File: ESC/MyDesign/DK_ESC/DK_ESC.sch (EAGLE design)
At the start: 61 parts, among them IC2 7805

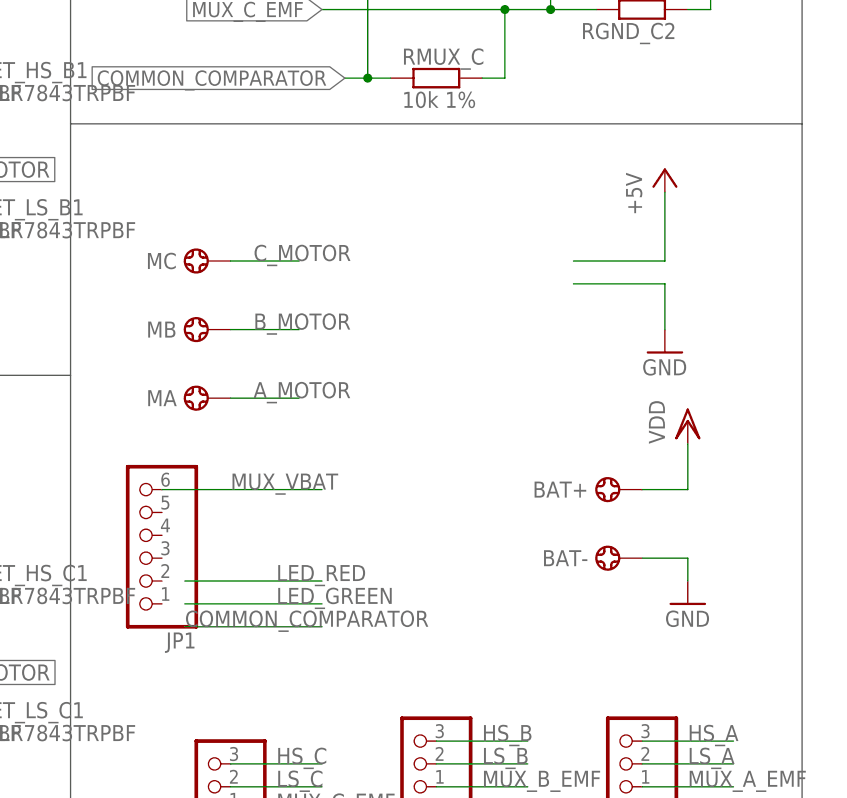
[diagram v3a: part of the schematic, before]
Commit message: Finish layout test ESC
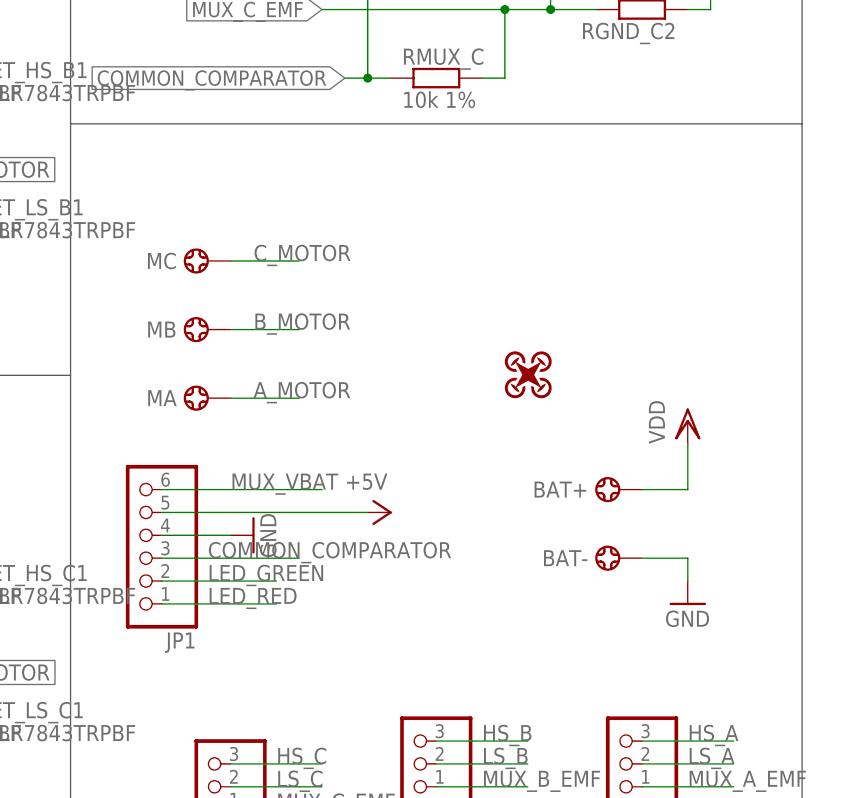
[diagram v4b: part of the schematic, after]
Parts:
- added U$2: QUADCOPTER-MEDIUM, logo:QUADCOPTER-MEDIUM
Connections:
- net +5V: now also JP1.5
- net COMMON_COMPARATOR: now also JP1.3
- net GND: now also JP1.4
- net LED_GREEN: now also JP1.2
- net LED_RED: now also JP1.1
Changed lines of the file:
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@@
 <part name="JP-C" library="pinhead" deviceset="PINHD-1X3" device=""/>
 <part name="JP1" library="pinhead" deviceset="PINHD-1X6" device=""/>
+<part name="U$2" library="logo" deviceset="QUADCOPTER" device="-MEDIUM"/>
 </parts>
 <sheets>
@@
 <instance part="MB" gate="G$1" x="96.52" y="-35.56" rot="R180"/>
 <instance part="MC" gate="G$1" x="96.52" y="-27.94" rot="R180"/>
-<instance part="GND11" gate="1" x="147.32" y="-38.1"/>
-<instance part="P+6" gate="1" x="147.32" y="-17.78"/>
+<instance part="GND11" gate="1" x="101.6" y="-58.42" rot="R90"/>
+<instance part="P+6" gate="1" x="116.84" y="-55.88" rot="R270"/>
 <instance part="FET_HS_A1" gate="G$1" x="66.04" y="45.72"/>
 <instance part="FET_LS_A1" gate="G$1" x="66.04" y="30.48"/>
@@
 <instance part="JP-C" gate="A" x="96.52" y="-86.36" rot="R180"/>
 <instance part="JP1" gate="A" x="88.9" y="-58.42" rot="R180"/>
+<instance part="U$2" gate="G$1" x="129.54" y="-43.18"/>
 </instances>
 <busses>
@@
 </segment>
 <segment>
-<wire x1="137.16" y1="-30.48" x2="147.32" y2="-30.48" width="0.1524" layer="91"/>
-<pinref part="GND11" gate="1" pin="GND"/>
-<wire x1="147.32" y1="-30.48" x2="147.32" y2="-35.56" width="0.1524" layer="91"/>
-</segment>
-<segment>
 <pinref part="C1" gate="G$1" pin="-"/>
 <wire x1="-7.62" y1="33.02" x2="-7.62" y2="30.48" width="0.1524" layer="91"/>
@@
 <wire x1="144.78" y1="-60.96" x2="149.86" y2="-60.96" width="0.1524" layer="91"/>
 <wire x1="149.86" y1="-60.96" x2="149.86" y2="-63.5" width="0.1524" layer="91"/>
+</segment>
+<segment>
+<pinref part="JP1" gate="A" pin="4"/>
+<pinref part="GND11" gate="1" pin="GND"/>
+<wire x1="99.06" y1="-58.42" x2="91.44" y2="-58.42" width="0.1524" layer="91"/>
 </segment>
 </net>
@@
 </segment>
 <segment>
-<wire x1="93.98" y1="-68.58" x2="109.22" y2="-68.58" width="0.1524" layer="91"/>
-<label x="93.98" y="-68.58" size="1.778" layer="95"/>
+<wire x1="91.44" y1="-60.96" x2="106.68" y2="-60.96" width="0.1524" layer="91"/>
+<label x="96.52" y="-60.96" size="1.778" layer="95"/>
+<pinref part="JP1" gate="A" pin="3"/>
 </segment>
 </net>
@@
 </segment>
 <segment>
-<wire x1="137.16" y1="-27.94" x2="147.32" y2="-27.94" width="0.1524" layer="91"/>
+<pinref part="JP1" gate="A" pin="5"/>
 <pinref part="P+6" gate="1" pin="+5V"/>
-<wire x1="147.32" y1="-20.32" x2="147.32" y2="-27.94" width="0.1524" layer="91"/>
+<wire x1="114.3" y1="-55.88" x2="91.44" y2="-55.88" width="0.1524" layer="91"/>
 </segment>
 </net>
@@
 </segment>
 <segment>
-<wire x1="93.98" y1="-66.04" x2="109.22" y2="-66.04" width="0.1524" layer="91"/>
-<label x="104.14" y="-66.04" size="1.778" layer="95"/>
+<wire x1="91.44" y1="-63.5" x2="104.14" y2="-63.5" width="0.1524" layer="91"/>
+<label x="96.52" y="-63.5" size="1.778" layer="95"/>
+<pinref part="JP1" gate="A" pin="2"/>
 </segment>
 </net>
@@
 </segment>
 <segment>
-<wire x1="93.98" y1="-63.5" x2="109.22" y2="-63.5" width="0.1524" layer="91"/>
-<label x="104.14" y="-63.5" size="1.778" layer="95"/>
-</segment>
-</net>
+<wire x1="91.44" y1="-66.04" x2="104.14" y2="-66.04" width="0.1524" layer="91"/>
+<label x="96.52" y="-66.04" size="1.778" layer="95"/>
+<pinref part="JP1" gate="A" pin="1"/>
+</segment>
+</net>

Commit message: Update logo renesas
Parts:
- removed U$2: QUADCOPTER-MEDIUM, logo:QUADCOPTER-MEDIUM
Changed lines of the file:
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@@
 <part name="JP-C" library="pinhead" deviceset="PINHD-1X3" device=""/>
 <part name="JP1" library="pinhead" deviceset="PINHD-1X6" device=""/>
-<part name="U$2" library="logo" deviceset="QUADCOPTER" device="-MEDIUM"/>
 </parts>
 <sheets>
@@
 <instance part="JP-C" gate="A" x="96.52" y="-86.36" rot="R180"/>
 <instance part="JP1" gate="A" x="88.9" y="-58.42" rot="R180"/>
-<instance part="U$2" gate="G$1" x="129.54" y="-43.18"/>
 </instances>
 <busses>
